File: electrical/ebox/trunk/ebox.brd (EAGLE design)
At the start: 127 x 101.6 mm, 158 parts, among them IC1 MAX3221CUE, IC10 SN74LVC1G125, IC11 MAX3221CUE, IC12 INA170, IC13 SN74LVC1G125, IC14 SN74LVC1G125, IC15 MAX3221CUE, IC16 MCP170333MB, IC17 SN74LVC1G125, IC18 SN74LVC1G125, IC19 74ALS04D, IC2 LT3652, IC3 XMEGA128A1, IC4 LT1161, IC5 SN74LVC1G125, IC6 SN74LVC1G125, IC7 MAX3221CUE, IC8 INA170, IC9 SN74LVC1G125, Q1 FDD4141TO252, U1 BLUETOOTH-RN42, U2 D2523T_, X1 7381-3PG-300, X10 DEANS-MALE, X11 B4B-ZR, X12 DEANS-MALE, X13 B4B-ZR, X14 22-23-2021, X15 DEANS-FEMALE, X16 DEANS-FEMALE, X17 USB_A, X2 7381-3PG-300, X3 7381-2PG-300, X4 17984-7PG-300, X5 17984-7PG-300, X6 17984-7PG-300, X7 17984-7PG-300, X8 22-23-2031, X9 22-23-2031

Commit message: Fixed sensor routing, couple of other things.
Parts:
- added C22: 10uF, rcl:C0805
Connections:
- net +12V: now also C22.1
- net GND: now also C22.2
- net GPIO1A: now also IC3.35; no longer IC3.25
- net GPIO1B: now also IC3.36; no longer IC3.26, IC3.8
- net GPIO2A: now also IC3.39; no longer IC3.29
- net GPIO2B: now also IC3.40, IC3.8; no longer IC3.30
- net GPIO3A: now also IC3.25; no longer IC3.35
- net GPIO3B: now also IC3.26; no longer IC3.36
- net GPIO4A: now also IC3.29; no longer IC3.39
- net GPIO4B: now also IC3.30; no longer IC3.40
- net RX1_TTL: now also IC3.37; no longer IC3.27
- net RX2_TTL: now also IC3.41; no longer IC3.31
- net RX3_TTL: now also IC3.27; no longer IC3.37
- net RX4_TTL: now also IC3.31; no longer IC3.41
- net TX1_TTL: now also IC3.38; no longer IC3.28
- net TX2_TTL: now also IC3.42; no longer IC3.32
- net TX3_TTL: now also IC3.28; no longer IC3.38
- net TX4_TTL: now also IC3.32; no longer IC3.42
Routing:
- net +5V: track 25.3 -> 126.7 mm, vias 1 -> 6
- net GND: track 239.6 -> 245.9 mm, vias 31 -> 34

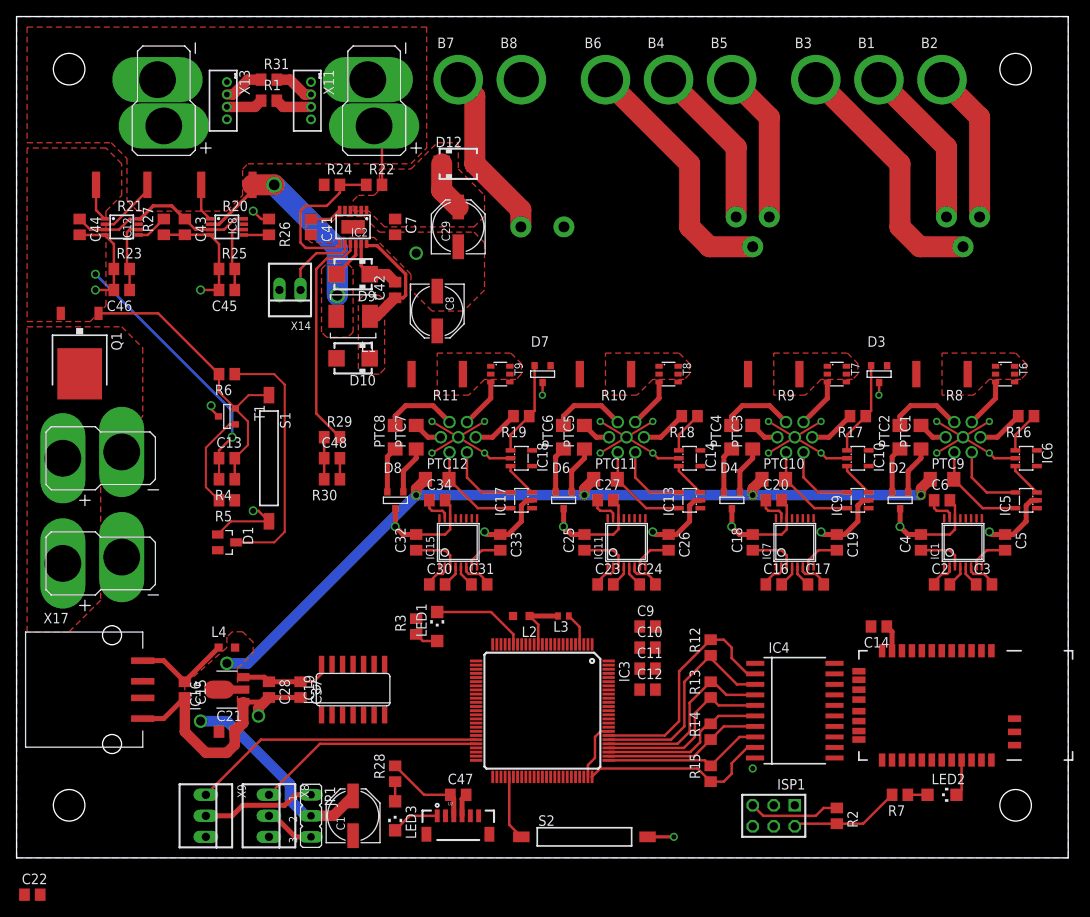
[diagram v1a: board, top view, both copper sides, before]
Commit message: More routing finished, under 100 airwires.
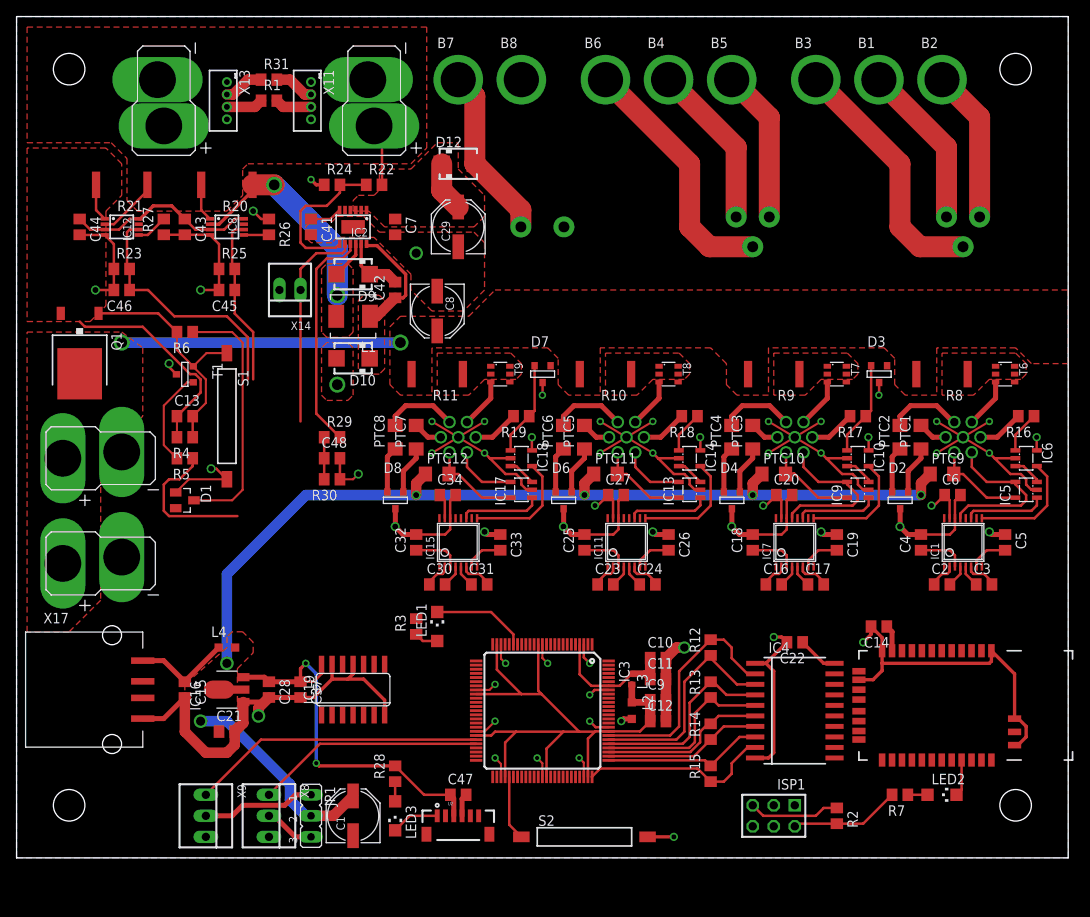
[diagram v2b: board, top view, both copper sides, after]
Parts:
- moved C22 97.0 mm to (94.0, 26.0), turned to 180 degrees
- moved L2 17.6 mm to (74.3, 17.8), turned to 270 degrees
- moved L3 11.2 mm to (74.3, 21.6), turned to 270 degrees
- moved C9 8.98 mm to (77.5, 19.1)
- moved S1 7.18 mm to (25.4, 53.3)
- moved C13 7.18 mm to (20.3, 53.3)
- moved D1 7.18 mm to (20.3, 43.2)
- moved R4 7.18 mm to (20.3, 50.8)
- moved R5 7.18 mm to (20.3, 48.3)
- moved R6 7.18 mm to (20.3, 63.5)
- moved T1 7.18 mm to (20.3, 58.4)
- moved C12 4.02 mm to (77.5, 16.5)
- moved C10 1.80 mm to (77.5, 24.1)
- moved C11 1.80 mm to (77.5, 21.6)
- moved C34 1.42 mm to (52.1, 43.8)
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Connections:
- net N$17 renamed 3ROU
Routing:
- net GND: track 245.9 -> 369.1 mm, vias 34 -> 50
- net AVR_VCC: track 14.7 -> 74.6 mm
- net +12V: track 0.00 -> 38.6 mm, vias 0 -> 2
- net +3V3: track 76.6 -> 112.9 mm, vias 0 -> 10
- net BATT_CURR_OUT: track 8.66 -> 30.4 mm
- net PWR_CTL: track 0.00 -> 17.7 mm
- net BATT_TEMP: track 9.66 -> 25.5 mm
- net RX3_TTL: track 0.00 -> 14.1 mm
- net RX4_TTL: track 0.00 -> 13.8 mm
- net RX2_TTL: track 0.00 -> 13.8 mm
- net RX1_TTL: track 0.00 -> 13.8 mm
- net AVR_AVCC: track 3.97 -> 16.1 mm
- net BATT_CURR_IN: track 8.66 -> 20.4 mm
- net S1_TX: track 9.05 -> 19.7 mm
- net S2_TX: track 9.05 -> 19.7 mm
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
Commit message: All high power routing is sufficient.  Tuning routing on digital lines.
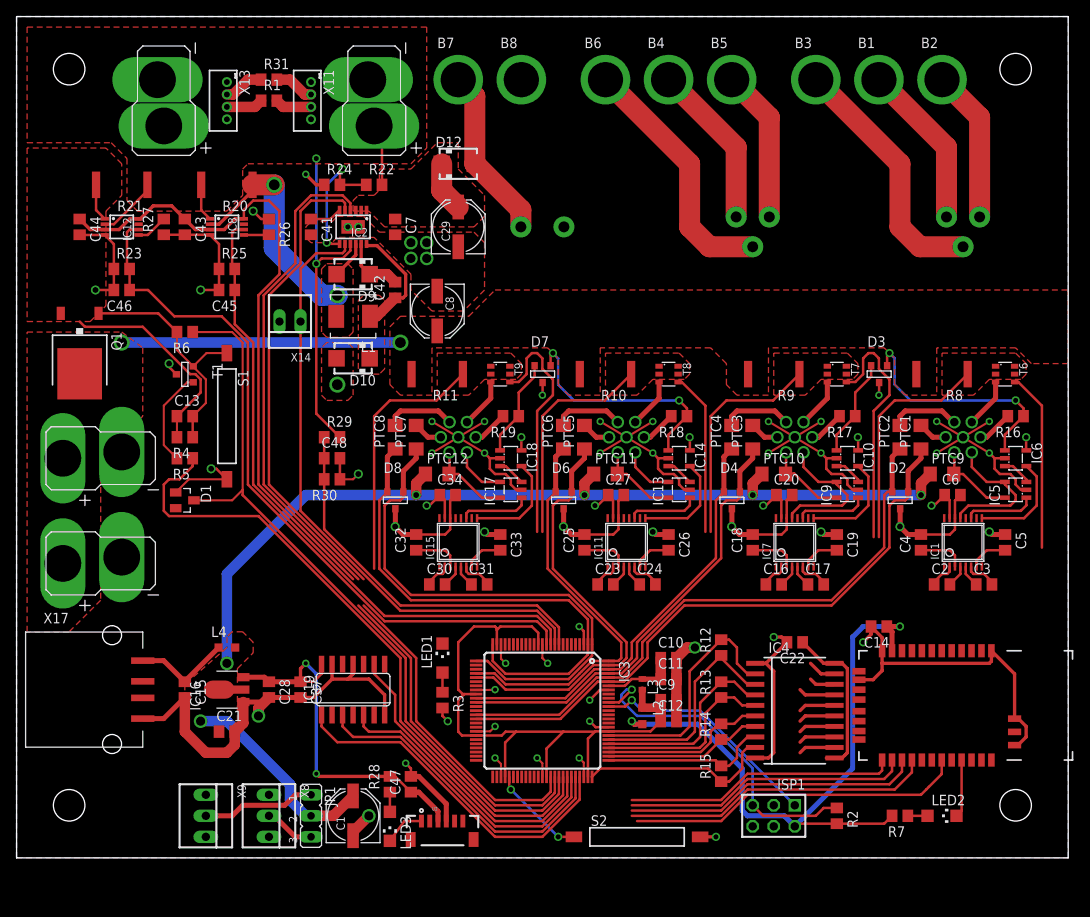
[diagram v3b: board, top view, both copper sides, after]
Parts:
- moved R3 9.44 mm to (51.4, 19.1), turned to 270 degrees
- moved S2 6.35 mm to (74.9, 2.54)
- moved C47 5.85 mm to (47.6, 8.89), turned to 90 degrees
- moved LED1 3.86 mm to (51.4, 24.1)
- moved X14 3.81 mm to (33.0, 64.8)
- moved LED2 2.54 mm to (111.8, 5.08)
- moved R7 2.54 mm to (106.7, 5.08)
- moved U2 2.01 mm to (48.9, 4.45)
- moved LED3 1.42 mm to (45.1, 3.81)
- moved R28 1.42 mm to (45.1, 8.89)
- moved L2 1.42 mm to (75.6, 17.1)
- moved L3 1.42 mm to (75.6, 21.0)
- moved R12 1.27 mm to (85.1, 25.4)
- moved R13 1.27 mm to (85.1, 20.3)
- moved R14 1.27 mm to (85.1, 15.2)
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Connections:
- net !CHRG: now also IC3.66; no longer IC3.68
- net !CHRG_FAULT: now also IC3.65; no longer IC3.67
- net !EN232_1: now also IC19.9; no longer IC19.1
- net !EN232_2: now also IC19.5; no longer IC19.3
- net !EN232_3: now also IC19.3; no longer IC19.5
- net !EN232_4: now also IC19.1; no longer IC19.9
- net BATT_CURR_IN: now also IC3.11; no longer IC3.95
- net BATT_CURR_OUT: now also IC3.12; no longer IC3.96
- net BATT_TEMP: now also IC3.10; no longer IC3.97
- net BATT_VSENSE: now also IC3.9; no longer IC3.98
- net BT_CTS: now also IC3.52; no longer IC3.49
- net BT_STATUS: now also IC3.49; no longer IC3.52
- net EN232_1: now also IC19.8; no longer IC19.2
- net EN232_2: now also IC19.6; no longer IC19.4
- net EN232_3: now also IC19.4; no longer IC19.6
- net EN232_4: now also IC19.2; no longer IC19.8
- net GPIO1A: now also IC3.40, IC3.95; no longer IC3.35, IC3.5
- net GPIO1B: now also IC3.39, IC3.96; no longer IC3.36, IC3.6
- net GPIO2A: now also IC3.36, IC3.97; no longer IC3.39, IC3.7
- net GPIO2B: now also IC3.35, IC3.98; no longer IC3.40, IC3.8
- net GPIO3A: now also IC3.30, IC3.99; no longer IC3.25, IC3.9
- net GPIO3B: now also IC3.100, IC3.29; no longer IC3.10, IC3.26
- net GPIO4A: now also IC3.1, IC3.26; no longer IC3.11, IC3.29
- net GPIO4B: now also IC3.2, IC3.25; no longer IC3.12, IC3.30
- net PWR_CTL: now also IC3.68; no longer IC3.56
- net PWR_SENSE: now also IC3.67; no longer IC3.57
- net RX1_TTL: now also IC3.41; no longer IC3.37
- net RX2_TTL: now also IC3.37; no longer IC3.41
- net RX3_TTL: now also IC3.31; no longer IC3.27
- net RX4_TTL: now also IC3.27; no longer IC3.31
- net TX1_TTL: now also IC3.42; no longer IC3.38
- net TX2_TTL: now also IC3.38; no longer IC3.42
- net TX3_TTL: now also IC3.32; no longer IC3.28
- net TX4_TTL: now also IC3.28; no longer IC3.32
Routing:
- net +3V3: track 112.9 -> 232.5 mm, vias 10 -> 13
- net !CHRG: track 0.00 -> 100.2 mm
- net !CHRG_FAULT: track 0.00 -> 96.6 mm
- net GPIO1A: track 5.82 -> 73.8 mm
- net GPIO1B: track 5.57 -> 71.8 mm
- net PWR_CTL: track 17.7 -> 79.7 mm
- net PWR_SENSE: track 30.8 -> 92.7 mm
- net GPIO4A: track 5.82 -> 64.9 mm
- net BATT_CURR_IN: track 20.4 -> 78.0 mm
- net BATT_CURR_OUT: track 30.4 -> 87.8 mm
- net GPIO4B: track 5.57 -> 62.3 mm
- net BATT_TEMP: track 25.5 -> 74.8 mm
- net GPIO2A: track 5.82 -> 53.4 mm
- net GPIO3A: track 5.82 -> 51.6 mm
- net GPIO2B: track 5.57 -> 51.0 mm
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
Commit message: Almost all digital routing completed and checked.  Need to do pwr ctrl and enable lines.
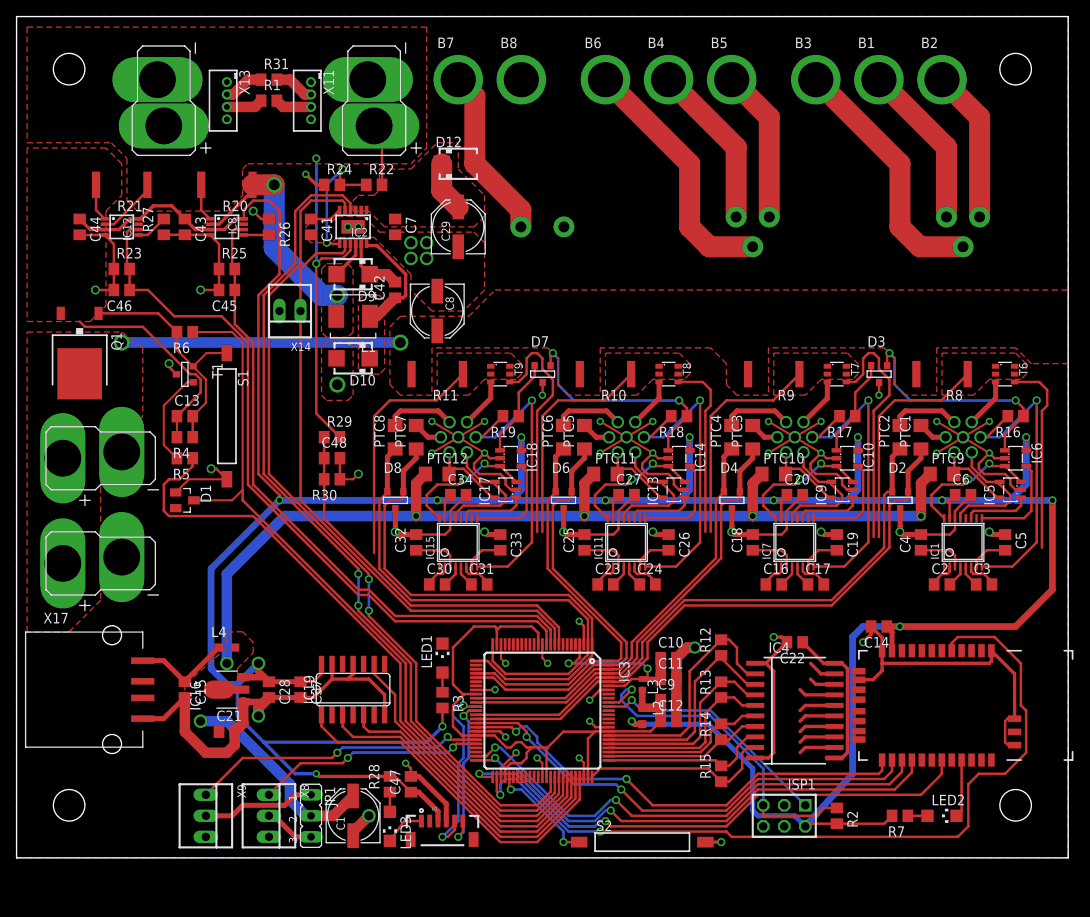
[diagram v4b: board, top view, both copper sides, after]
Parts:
- moved C20 1.27 mm to (94.0, 43.8)
- moved X14 1.27 mm to (33.0, 66.0)
- moved C34 1.27 mm to (53.3, 43.8)
- moved C27 1.27 mm to (73.7, 43.8)
- moved C6 1.27 mm to (114.3, 43.8)
- moved ISP1 1.27 mm to (92.7, 5.08)
- moved S2 0.90 mm to (75.6, 1.91)
- moved IC13 0.64 mm to (79.4, 44.5)
- moved IC5 0.64 mm to (120.0, 44.5)
- moved IC9 0.64 mm to (99.7, 44.5)
- moved IC17 0.63 mm to (59.1, 44.5)
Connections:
- net BT_CTS: now also IC3.50; no longer IC3.52
- net BT_RESET: now also IC3.52; no longer IC3.51
- net BT_RTS: now also IC3.49; no longer IC3.50
- net BT_RXD: now also IC3.41; no longer IC3.21
- net BT_STATUS: now also IC3.51; no longer IC3.49
- net BT_TXD: now also IC3.42; no longer IC3.22
- net GPS_RXD: now also IC3.37; no longer IC3.17
- net GPS_TXD: now also IC3.38; no longer IC3.18
- net RX1_TTL: now also IC3.17; no longer IC3.41
- net RX2_TTL: now also IC3.21; no longer IC3.37
- net TX1_TTL: now also IC3.18; no longer IC3.42
- net TX2_TTL: now also IC3.22; no longer IC3.38
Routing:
- net +3V3: track 232.5 -> 427.6 mm, vias 13 -> 15
- net BT_RESET: track 0.00 -> 99.4 mm, vias 0 -> 2
- net MOT2_SIG: track 0.00 -> 35.7 mm, vias 0 -> 2
- net S3_RX: track 4.34 -> 37.9 mm, vias 0 -> 1
- net S2_RX: track 4.34 -> 37.9 mm, vias 0 -> 1
- net S1_RX: track 4.34 -> 37.9 mm, vias 0 -> 1
- net S4_RX: track 4.34 -> 37.9 mm, vias 0 -> 1
- net MOT1_SIG: track 0.00 -> 27.6 mm, vias 0 -> 2
- net BT_RTS: track 36.0 -> 60.5 mm, vias 0 -> 2
- net BT_STATUS: track 40.8 -> 65.1 mm, vias 0 -> 2
- net BT_TXD: track 33.0 -> 56.8 mm, vias 0 -> 2
- net BT_RXD: track 34.5 -> 58.3 mm, vias 0 -> 2
- net BT_CTS: track 37.5 -> 60.9 mm, vias 0 -> 2
- net GPS_RXD: track 0.00 -> 22.8 mm, vias 0 -> 2
- net GPS_TXD: track 0.00 -> 19.3 mm, vias 0 -> 2
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
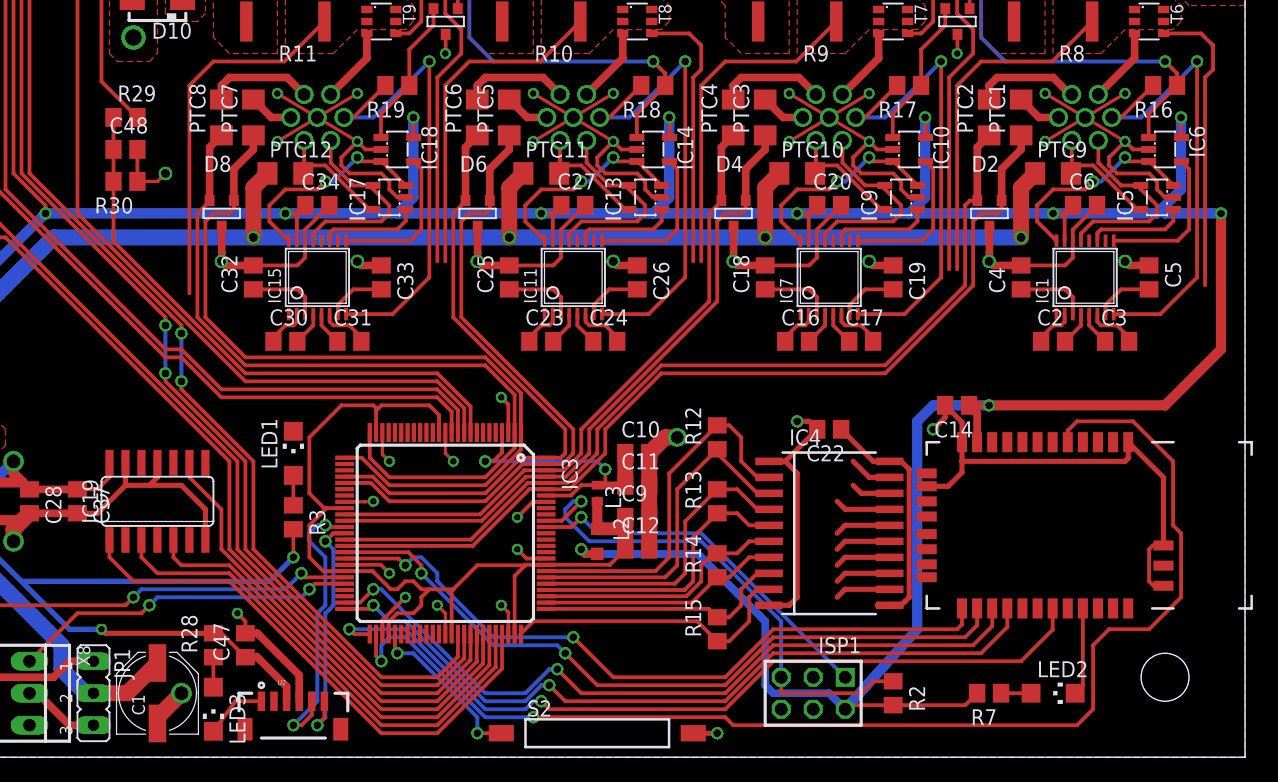
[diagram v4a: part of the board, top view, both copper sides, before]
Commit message: All signal wiring to MCU stable.  Just need to do enable lines and clean up.
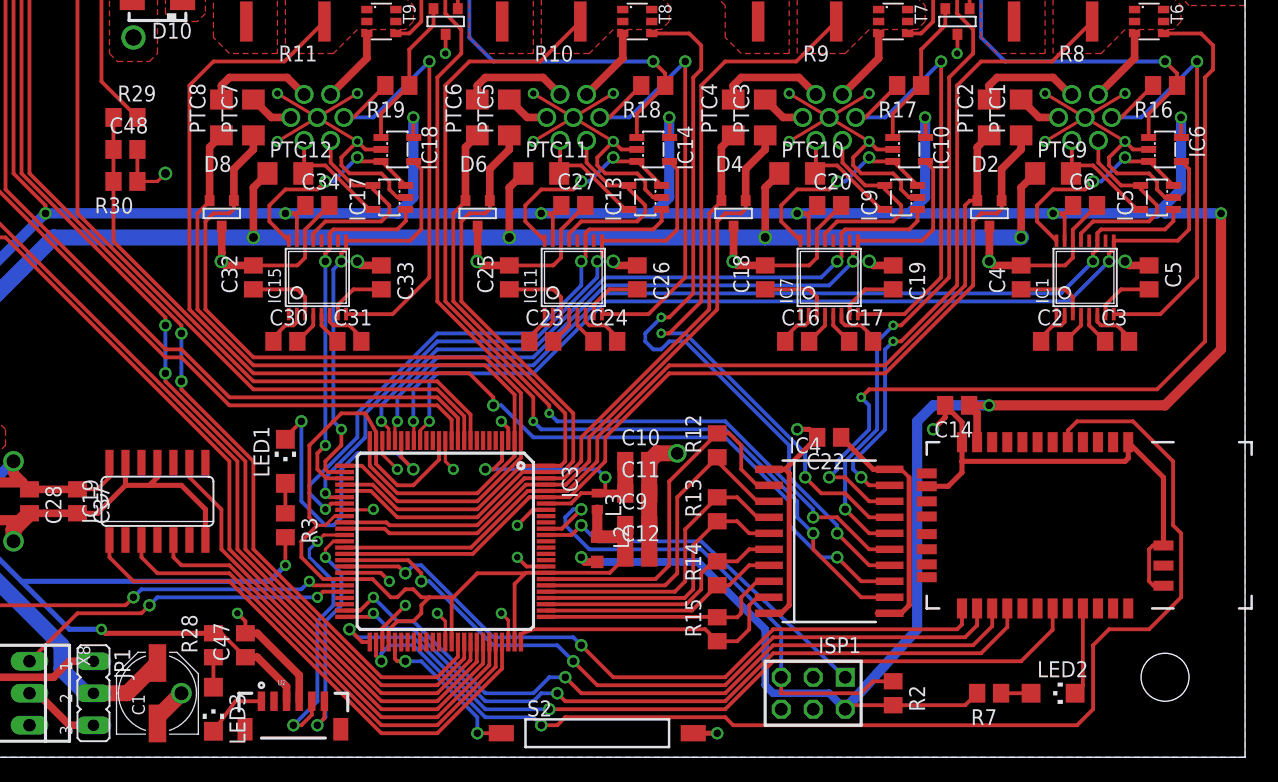
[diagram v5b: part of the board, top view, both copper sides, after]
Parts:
- moved R3 0.90 mm to (50.8, 18.4)
- moved LED1 0.90 mm to (50.8, 23.5)
- moved C11 0.64 mm to (78.7, 21.0)
- moved C12 0.64 mm to (78.7, 15.9)
- moved C22 0.64 mm to (94.0, 25.4)
- moved C9 0.64 mm to (78.7, 18.4)
- moved IC3 0.64 mm to (63.5, 17.1)
- moved IC4 0.64 mm to (94.0, 17.1)
- moved R13 0.64 mm to (85.1, 19.7)
- moved R14 0.63 mm to (85.1, 14.6)
- moved C10 0.63 mm to (78.7, 23.5)
- moved L2 0.63 mm to (75.6, 16.5)
- moved L3 0.63 mm to (75.6, 20.3)
- moved R12 0.63 mm to (85.1, 24.8)
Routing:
- net RX1_TTL: track 12.0 -> 76.7 mm, vias 0 -> 2
- net TX1_TTL: track 7.96 -> 72.1 mm, vias 0 -> 2
- net N$16: track 33.8 -> 96.6 mm, vias 0 -> 2
- net N$20: track 33.5 -> 80.5 mm, vias 0 -> 2
- net RX2_TTL: track 12.0 -> 58.0 mm, vias 0 -> 2
- net TX2_TTL: track 7.96 -> 53.7 mm, vias 0 -> 2
- net 3ROU: track 27.2 -> 71.2 mm, vias 0 -> 2
- net N$15: track 31.2 -> 74.1 mm, vias 0 -> 2
- net TX3_TTL: track 7.96 -> 45.1 mm, vias 0 -> 2
- net RX3_TTL: track 12.3 -> 47.6 mm, vias 0 -> 2
- net N$19: track 26.6 -> 59.6 mm, vias 0 -> 2
- net N$14: track 31.2 -> 59.5 mm, vias 0 -> 2
- net LED_STATUS: track 0.00 -> 25.8 mm, vias 0 -> 2
- net N$18: track 34.1 -> 56.8 mm, vias 0 -> 2
- net TX4_TTL: track 7.96 -> 29.0 mm, vias 0 -> 2
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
